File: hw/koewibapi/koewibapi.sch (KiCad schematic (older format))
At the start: 84 parts, among them J1 POWER IN 24V, J10 IN0, J11 IN1, J12 IN2, J13 IN3, J14 IN4, J15 IN5, J16 IN6, J17 IN7, J18 Terminate Bus, J19 Bus Pull-Up, J2 BUS_24V, J20 Bus Pull-Down, J21 Activate output LEDs, J22 Activate Input LEDs, J23 unused GPIO Pins, J24 Input Signals, J25 unused RPi Rins, J26 CONN_RASPI_REV2, J3 CONN_1X1, J4 CONN_1X1, J5 BUS_GND, J6 REL0, J7 REL1, J8 REL2, J9 REL3, SW1 MAIN, SW2 24V BUS, SW3 5V RASPI, SW4 5V LOGIC, U1 LM2576, U2 32.768kHz, U3 MAX487, U4 MCP23016, U5 DS1307, U6 PCA9517

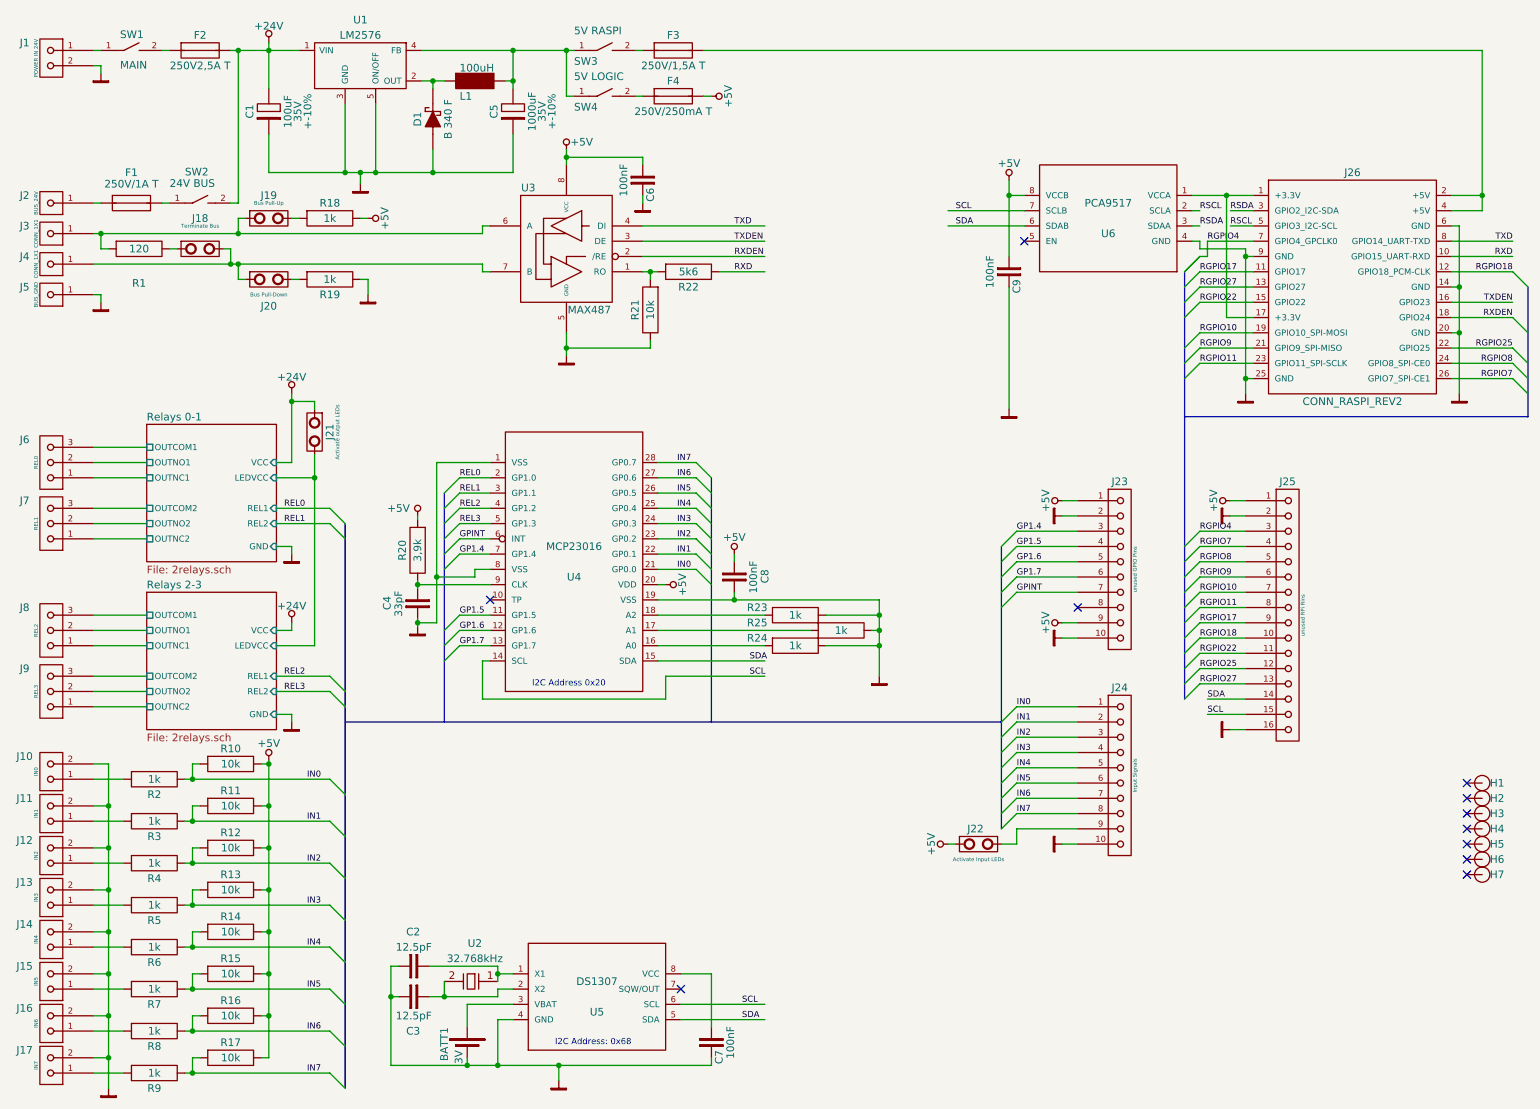
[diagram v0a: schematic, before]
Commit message: Initial revision of layout of KOEWIBA-PI. Gerber files also added.
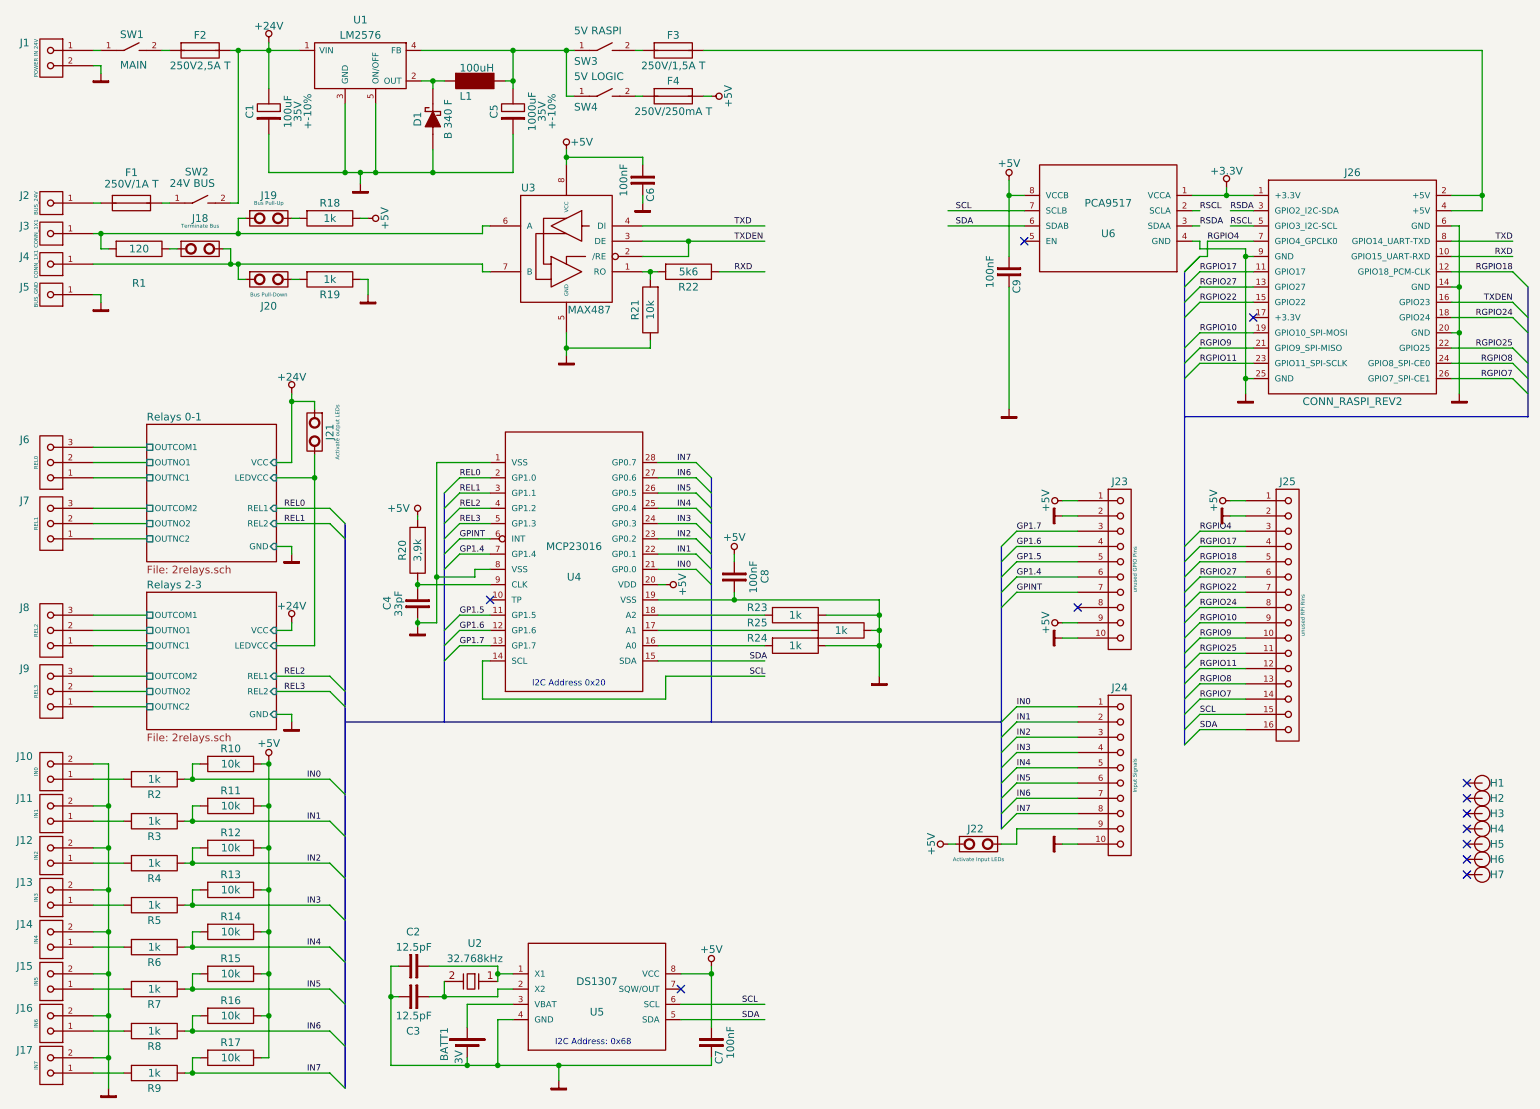
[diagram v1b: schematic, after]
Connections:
- net +5V: now also C7.1, U5.8 (VCC)
- net GND: no longer J25.16
- net GP1.4: now also J23.6; no longer J23.3
- net GP1.5: now also J23.5; no longer J23.4
- net GP1.6: now also J23.4; no longer J23.5
- net GP1.7: now also J23.3; no longer J23.6
- net RGPIO10: now also J25.9; no longer J25.7
- net RGPIO11: now also J25.12; no longer J25.8
- net RGPIO17: now also J25.4; no longer J25.9
- net RGPIO18: now also J25.5; no longer J25.10
- net RGPIO22: now also J25.7; no longer J25.11
- net RGPIO25: now also J25.11; no longer J25.12
- net RGPIO27: now also J25.6; no longer J25.13
- net RGPIO7: now also J25.14; no longer J25.4
- net RGPIO8: now also J25.13; no longer J25.5
- net RGPIO9: now also J25.10; no longer J25.6
- net SDA: now also J25.16; no longer J25.14
- net TXDEN: now also U3.2 (/RE)
- net +3.3V: now reaches J26.1 (+3.3V), U6.1 (VCCA)
- net +3.3V: no longer J26.17 (+3.3V)
- net RXDEN renamed RGPIO24
- net RGPIO24: now also J25.8; no longer U3.2 (/RE)
- no-connect marks 11 -> 12

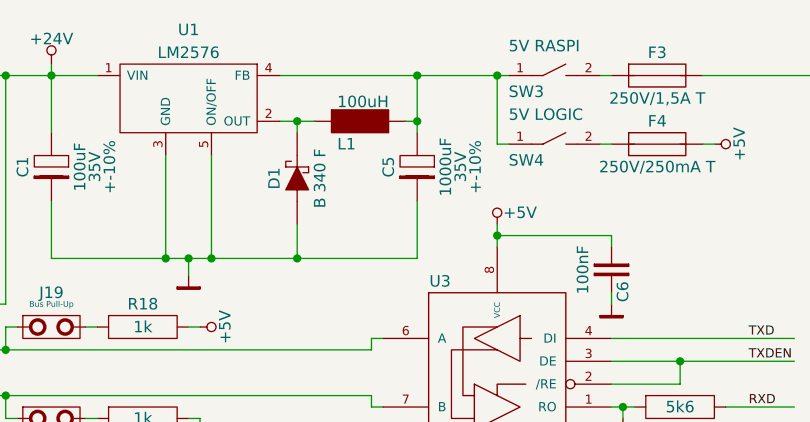
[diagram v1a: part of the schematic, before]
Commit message: - fixed space issues in layout - L1 value changed
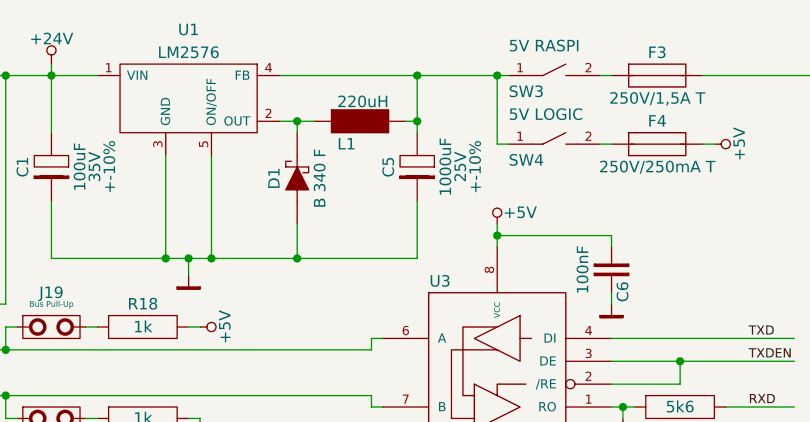
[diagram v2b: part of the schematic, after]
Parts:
- C5: Voltage 35V -> 25V
- L1: value 100uH -> 220uH
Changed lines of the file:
@@
-EESchema Schematic File Version 2  date Fr 27 Dez 2013 21:16:19 CET
+EESchema Schematic File Version 2  date Do 02 Jan 2014 12:24:19 CET
 LIBS:connectors
 LIBS:power
@@
 Sheet 1 3
 Title "KoeWiBaPi"
-Date "27 dec 2013"
+Date "2 jan 2014"
 Rev "1"
 Comp ""
@@
 F 0 "C5" H 4050 1025 50  0000 C CNN
 F 1 "1000uF" H 4050 1275 50  0000 C CNN
-F 4 "35V" H 4050 1340 50  0000 C CNN "Voltage"
+F 4 "25V" H 4050 1340 50  0000 C CNN "Voltage"
 F 5 "+-10%" H 4050 1405 50  0000 C CNN "Tolrance"
 	1    4050 1150
@@
 P 3800 950
 F 0 "L1" H 3700 850 50  0000 L CNN
-F 1 "100uH" H 3700 1035 50  0000 L CNN
+F 1 "220uH" H 3700 1035 50  0000 L CNN
 	1    3800 950
 	1    0    0    -1
